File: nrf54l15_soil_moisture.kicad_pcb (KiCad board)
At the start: 4 copper layers, 44.4 x 34 mm, 60 parts, among them CN1 SM04B-SRSS-TB, J2 TC2030, J3 USB_C_Receptacle_PowerOnly_6P, U1 nRF54L15-QDXX, U2 nPM1300-QEXX, U3 SPV1040T, U4 S2B-PH-K-S-GW, X1 XL7EL89CKI-111YLC-32M

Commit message: Save workspace changes
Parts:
- added D2: SS14_C83852, easyeda2kicad:SMA_L4.3-W2.6-LS5.2-RD, F.Cu at (119.9, 77.1)
- added U5: S2B-PH-K-S-GW, easyeda2kicad:CONN-TH_S2B-PH-K-S-GW, F.Cu at (110.8, 74.6)
- L1: value SDFL2012S100KTF -> 10uh
- R6: value 3.9M -> 3.01M
- moved R3 12.2 mm to (133.8, 72.9)
- moved R7 11.3 mm to (131.2, 76.2)
- moved R6 11.2 mm to (129.8, 76.2)
- moved U3 11.2 mm to (127.5, 72.4)
- moved C2 10.8 mm to (126.9, 77.8)
- moved D1 10.1 mm to (123.4, 77.9)
- moved L1 7.91 mm to (116.4, 78.1)
- moved C28 7.57 mm to (121.8, 71.0), turned to 90 degrees
- moved C27 7.47 mm to (116.3, 74.0), turned to 90 degrees
- moved R5 6.70 mm to (119.3, 70.4)
- moved R4 6.52 mm to (116.8, 70.4)
- moved AE1 3.71 mm to (135.0, 89.3), turned to 0 degrees
- moved J2 2.42 mm to (121.2, 97.1)
- moved R2 2.06 mm to (104.3, 76.0)
- moved R1 2.05 mm to (104.2, 74.0)
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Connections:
- C27 pad 1: SOLAR_5p5V -> GND
- C27 pad 2: GND -> SOLAR_5p5V
- J3 pad A1: (no net) -> GND
- J3 pad A4: (no net) -> VBUS
- J3 pad B1: (no net) -> GND
- J3 pad B4: (no net) -> VBUS
- L1 pad 2: SPV1040T_VOUT -> Net-(U3-LX)
- R4 pad 1: SPV1040T_VOUT -> SOLAR_5p5V
- U3 pad 3: SPV1040T_VOUT -> Net-(U3-LX)
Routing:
- net VOUT1: track 11.7 -> 89.8 mm, vias 0 -> 5
- net VBUS: track 8.43 -> 41.8 mm, vias 0 -> 2
- net nRF54_RESET: track 0.00 -> 20.6 mm, vias 0 -> 2
- net nRF54_SWDCLK: track 0.00 -> 20.5 mm, vias 0 -> 2
- net VBAT: track 4.61 -> 23.0 mm, vias 1 -> 3
- net SOLAR_5p5V: track 1.71 -> 19.9 mm
- net VOUT2: track 3.09 -> 20.6 mm, vias 0 -> 2
- net /npm1300/VSYS: track 15.5 -> 32.8 mm, vias 2 -> 3
- net GND: track 0.00 -> 15.2 mm, vias 16 -> 60
- net Net-(U3-LX): track 0.00 -> 11.5 mm
- net nRF54_SWDIO: track 0.00 -> 9.99 mm, vias 0 -> 2
- net I2C_SDA: track 26.0 -> 34.4 mm, vias 2 -> 4
- net ANT_SEL: track 0.89 -> 8.56 mm
- net Net-(U1-DECA): track 4.99 -> 9.81 mm, vias 0 -> 2
- net Net-(AE1-ANT): track 0.00 -> 2.94 mm
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- removed copper zone on In2.Cu, net VBAT

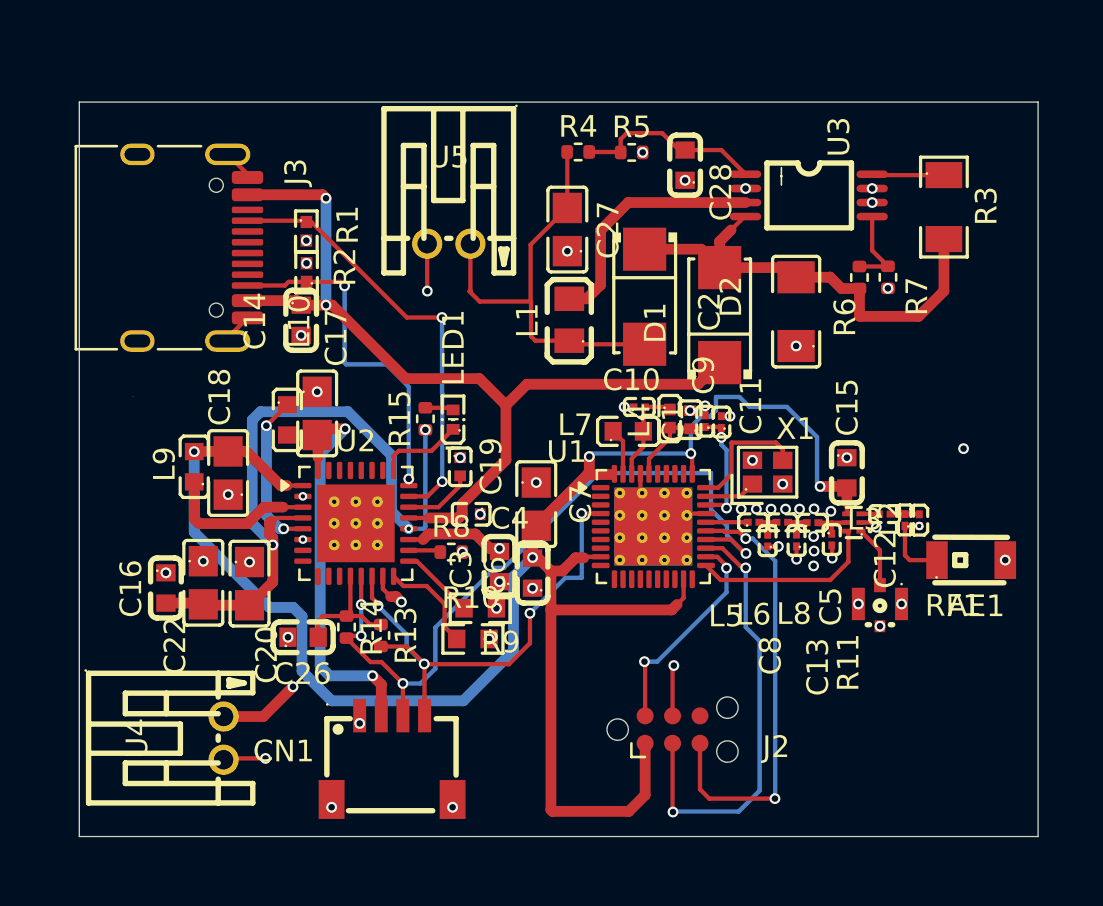
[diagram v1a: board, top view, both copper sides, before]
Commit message: Update soil moisture design and ignore KiCad lock files
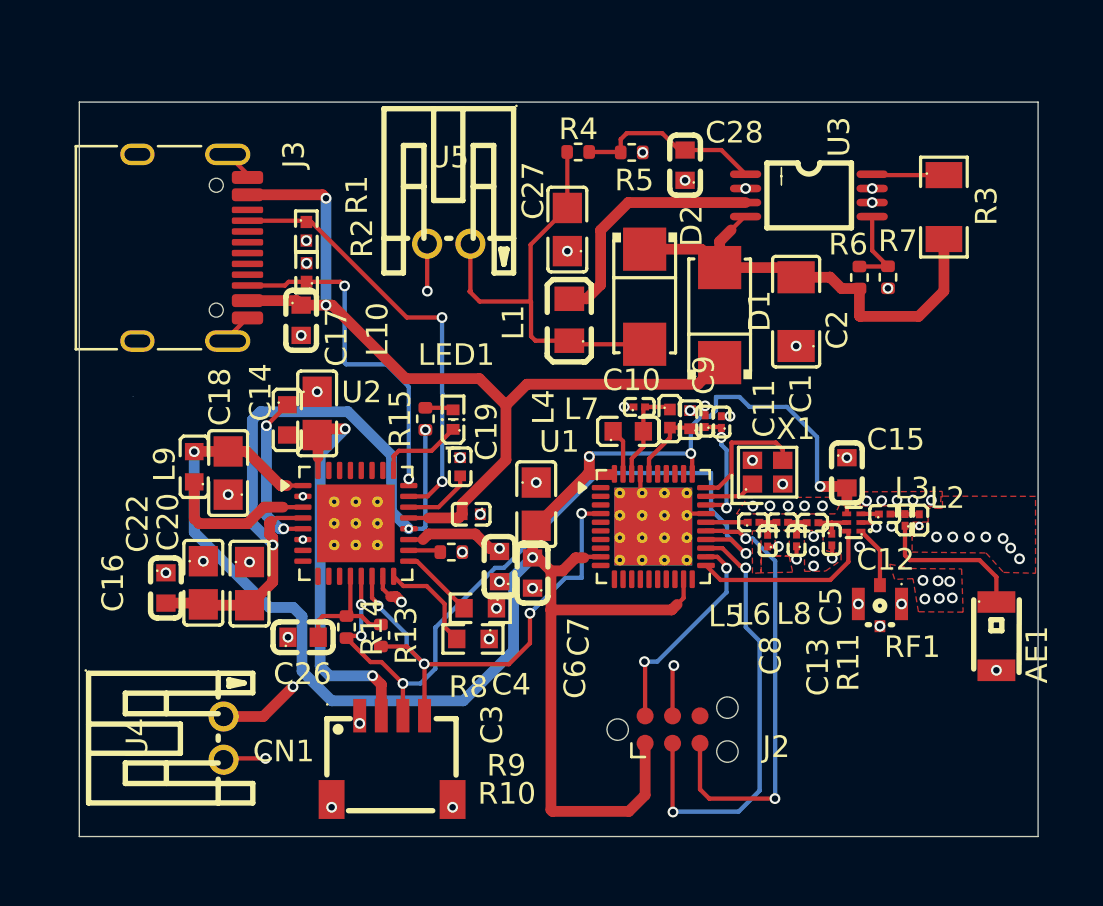
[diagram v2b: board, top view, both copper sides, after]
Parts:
- moved AE1 3.71 mm to (136.2, 92.8), turned to -90 degrees
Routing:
- net Net-(AE1-ANT): track 2.94 -> 7.17 mm
- net GND: vias 60 -> 77
- added copper zone on F.Cu, net GND

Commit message: Push remaining soil moisture PCB changes
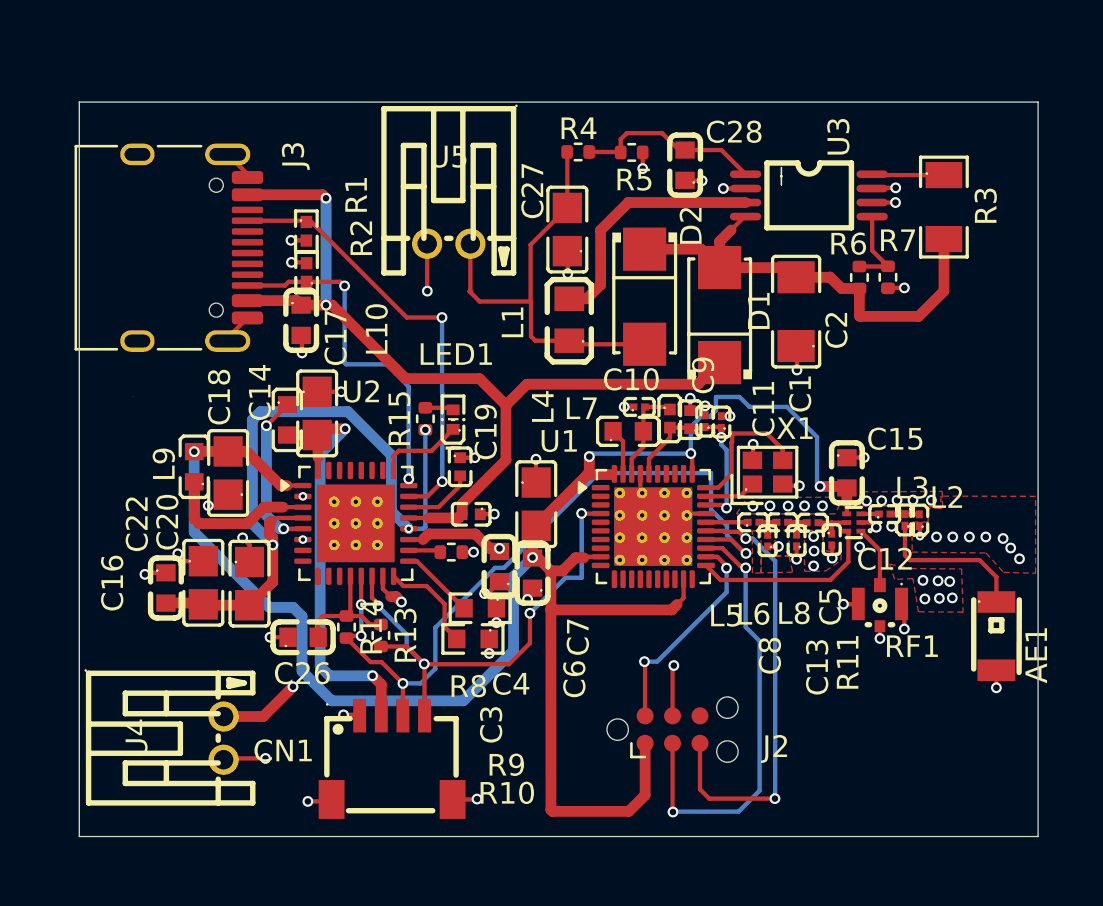
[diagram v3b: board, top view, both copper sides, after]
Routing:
- net GND: track 15.2 -> 47.3 mm
- net Net-(U1-XC2): track 5.91 -> 6.49 mm

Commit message: Push current KiCad workspace changes
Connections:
- C17 pad 2: VOUT2 -> VDDIO
- C6 pad 2: VOUT1 -> VDDIO
- C7 pad 2: VOUT1 -> VDDIO
- CN1 pad 2: VOUT2 -> VDDIO
- J2 pad 1: VOUT1 -> VDDIO
- J2 pad 3: nRF54_SWDCLK -> nRF54_RESET
- J2 pad 4: GND -> nRF54_SWDCLK
- J2 pad 5: nRF54_RESET -> GND
- L10 pad 2: VOUT2 -> VDDIO
- U1 pad 19: VOUT1 -> VDDIO
- U1 pad 20: unconnected-(U1-P0.00-Pad20) -> PMIC_INT
- U1 pad 24: I2C_SDA -> unconnected-(U1-P0.04-Pad24)
- U1 pad 31: VOUT1 -> VDDIO
- U1 pad 40: VOUT1 -> VDDIO
- U1 pad 5: unconnected-(U1-P1.04-Pad5) -> I2C_SDA
- U1 pad 9: VOUT1 -> VDDIO
- U2 pad 15: VBAT -> unconnected-(U2-SHPHLD-Pad15)
- U2 pad 32: VOUT2 -> VDDIO
- U2 pad 8: unconnected-(U2-GPIO1-Pad8) -> PMIC_INT
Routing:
- net VDDIO: track 5.83 -> 76.9 mm, vias 0 -> 7
- net VOUT1: track 89.8 -> 43.8 mm, vias 5 -> 2
- net PMIC_INT: track 0.00 -> 27.5 mm, vias 0 -> 2
- net VOUT2: track 20.6 -> 0.00 mm, vias 2 -> 0
- net I2C_SDA: track 34.4 -> 22.0 mm
- net nRF54_SWDCLK: track 20.5 -> 11.3 mm
- net nRF54_RESET: track 20.6 -> 23.0 mm
- net VBAT: track 23.0 -> 20.6 mm, vias 3 -> 2
- net GND: track 47.3 -> 46.7 mm, vias 77 -> 78

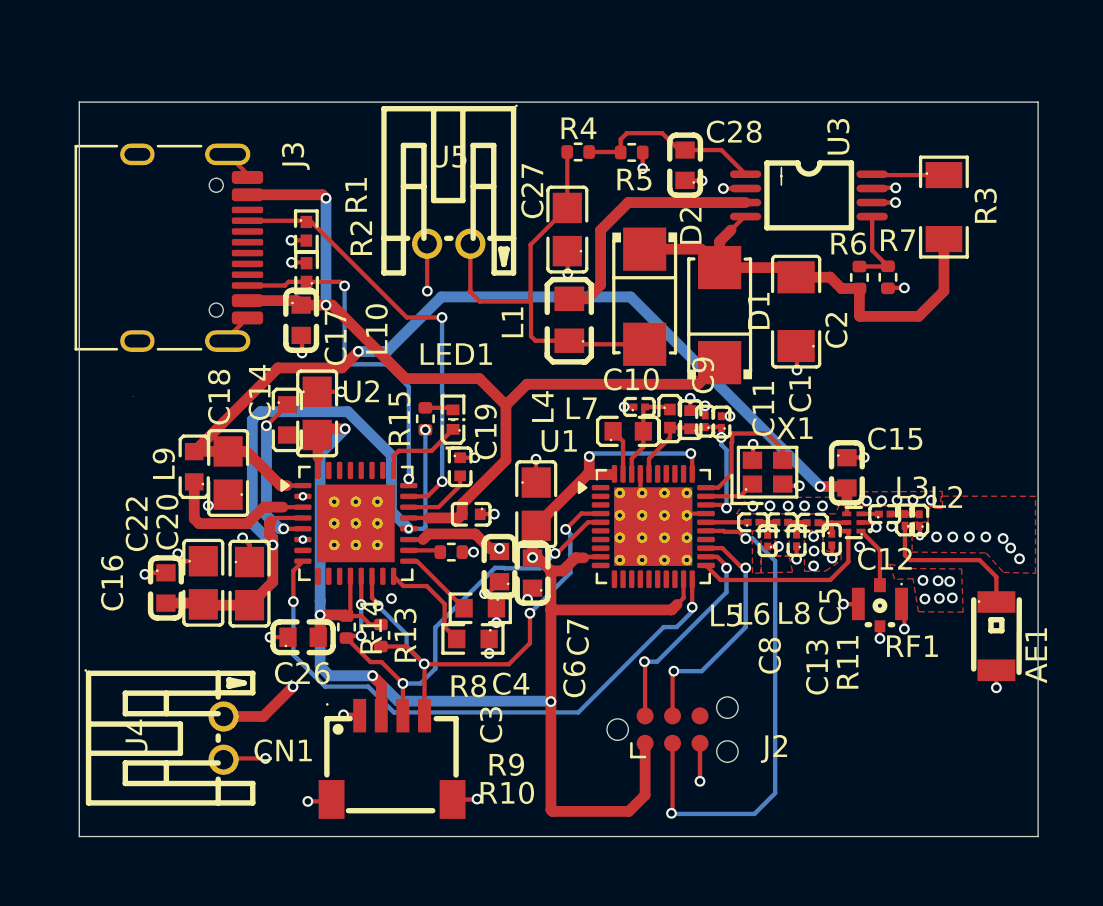
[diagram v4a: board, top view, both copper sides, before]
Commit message: Update nRF54L15 schematic, PCB layout, and project configuration
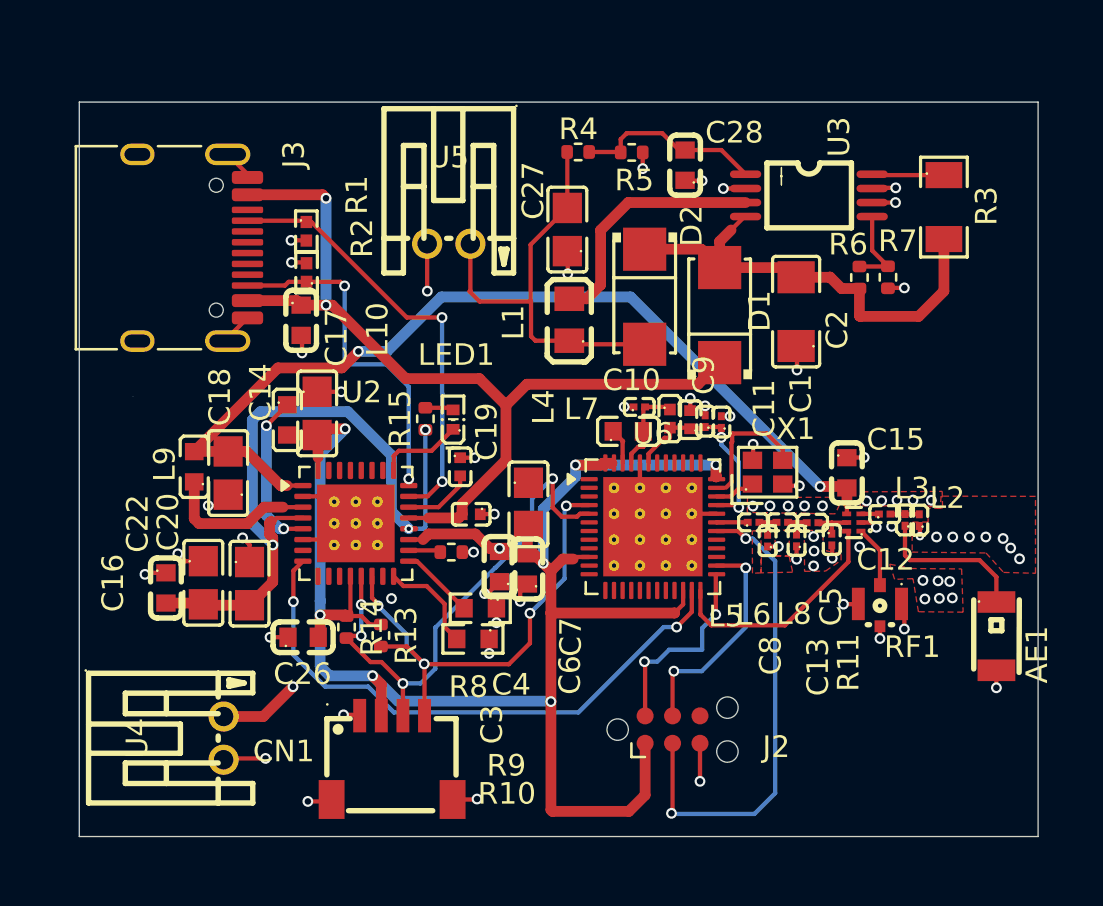
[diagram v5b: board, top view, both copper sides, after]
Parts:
- removed U1: nRF54L15-QDXX, Package_DFN_QFN:QFN-40-1EP_5x5mm_P0.4mm_EP3.6x3.6mm_ThermalVias
- added U6: nRF54L15-QFXX, Package_DFN_QFN:QFN-48-1EP_6x6mm_P0.4mm_EP4.6x4.6mm_ThermalVias, F.Cu at (120.3, 87.7)
- moved C7 0.36 mm to (114.5, 86.7)
- moved C6 0.31 mm to (114.5, 89.7)
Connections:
- J3 pad A1: GND -> (no net)
- J3 pad A4: VBUS -> (no net)
- J3 pad B1: GND -> (no net)
- J3 pad B4: VBUS -> (no net)
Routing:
- net GND: track 46.7 -> 51.8 mm, vias 78 -> 75
- net I2C_SDA: track 22.0 -> 24.7 mm
- net VDDIO: track 76.9 -> 79.3 mm
- net ANT_SEL: track 8.56 -> 10.7 mm
- net nRF54_SWDIO: track 9.99 -> 9.19 mm
- net nRF54_SWDCLK: track 11.3 -> 10.5 mm
- net Net-(U6-XC2): track 6.49 -> 5.77 mm
- net PMIC_INT: track 27.5 -> 27.0 mm

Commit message: Update schematic and PCB files
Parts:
- removed R15: 560, Resistor_SMD:R_0402_1005Metric
- added R12: 4.7k, easyeda2kicad:R0402, F.Cu at (107.6, 92.3)
- R1, R2: footprint EasyEDA2Kicad:R0402 -> easyeda2kicad:R0402
- R13, R4, R5, R6, R7, R8: footprint Resistor_SMD:R_0402_1005Metric -> easyeda2kicad:R0402
- R14: value 4.7k -> 560; footprint Resistor_SMD:R_0402_1005Metric -> easyeda2kicad:R0402
- moved R14 10.9 mm to (109.8, 82.1)
- moved R2 1.96 mm to (104.2, 74.0)
- moved R1 1.87 mm to (104.2, 75.9)
- moved R13 1.76 mm to (106.0, 92.2), turned to 90 degrees
- turned R5 to 180 degrees
- turned R6 to -90 degrees
- turned R7 to 90 degrees
- turned R8 to 180 degrees
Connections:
- R1 pad 1: CC1 -> GND
- R1 pad 2: GND -> CC2
- R13 pad 1: VDDIO -> I2C_SDA
- R13 pad 2: I2C_SCL -> VDDIO
- R14 pad 1: VDDIO -> Net-(LED1-A)
- R14 pad 2: I2C_SDA -> /npm1300/VSYS
- R2 pad 1: CC2 -> GND
- R2 pad 2: GND -> CC1
- R4 pad 1: SOLAR_5p5V -> Net-(U3-MPP-SET)
- R4 pad 2: Net-(U3-MPP-SET) -> SOLAR_5p5V
- R5 pad 1: Net-(U3-MPP-SET) -> GND
- R5 pad 2: GND -> Net-(U3-MPP-SET)
- R6 pad 1: SPV1040T_VOUT -> Net-(U3-VCTRL)
- R6 pad 2: Net-(U3-VCTRL) -> SPV1040T_VOUT
- R7 pad 1: Net-(U3-VCTRL) -> GND
- R7 pad 2: GND -> Net-(U3-VCTRL)
- R8 pad 1: Net-(U2-NTC) -> GND
- R8 pad 2: GND -> Net-(U2-NTC)
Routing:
- net I2C_SCL: track 23.3 -> 22.4 mm, vias 4 -> 3
- net /npm1300/VSYS: track 32.8 -> 33.5 mm
- net VDDIO: track 79.3 -> 80.0 mm, vias 7 -> 8
- net I2C_SDA: track 24.7 -> 24.5 mm, vias 4 -> 2

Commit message: Update KiCad schematic and PCB files
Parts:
- removed J3: USB_C_Receptacle_PowerOnly_6P, Connector_USB:USB_C_Receptacle_HRO_TYPE-C-31-M-12
- added J1: TYPE-C-31-M-12, easyeda2kicad:USB-C_SMD-TYPE-C-31-M-12_1, F.Cu at (99.0, 74.8)
- moved AE1 1.62 mm to (136.2, 94.4)
- turned D1 to -90 degrees
- turned D2 to 90 degrees
- turned R4 to 180 degrees
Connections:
- C2 pad 2: SPV1040T_VOUT -> CHG_IN
- C4 pad 2: VBUS -> CHG_IN
- D1 pad 1: VBUS -> CHG_IN
- D1 pad 2: SPV1040T_VOUT -> VBUS
- D2 pad 1: SPV1040T_VOUT -> CHG_IN
- R3 pad 2: SPV1040T_VOUT -> CHG_IN
- R6 pad 2: SPV1040T_VOUT -> CHG_IN
- U2 pad 21: VBUS -> CHG_IN
- U3 pad 4: SPV1040T_VOUT -> CHG_IN
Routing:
- net CHG_IN: track 0.00 -> 38.9 mm, vias 0 -> 2
- net SPV1040T_VOUT: track 21.7 -> 0.00 mm
- net VBUS: track 41.8 -> 32.4 mm
- net SOLAR_5p5V: track 19.9 -> 22.3 mm
- net GND: track 51.8 -> 53.8 mm, vias 75 -> 76
- net Net-(AE1-ANT): track 7.17 -> 8.80 mm
- net VDDIO: track 80.0 -> 80.7 mm
